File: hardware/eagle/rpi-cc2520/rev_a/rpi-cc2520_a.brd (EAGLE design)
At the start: 30.5 x 39.5 mm, 11 parts, among them J1 PINHD-2X12/SMD, J2 PINHD-2X12/SMD

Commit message: adding cc2520 and related parts
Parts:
- added C1: 1uF, rcl:C0603
- added C2, C3, C4: 100nF, rcl:C0402
- added JP2: (no value), pinhead:2X13
- added L1: (no value), SparkFun-Passives:0603
- added U1: CC2520, chips:S-PVQFN-N28
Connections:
- new net N$4: C1.1, C2.1, C3.1, C4.1, L1.1, U1.11, U1.14, U1.16, U1.20, U1.22, U1.24
- new net N$5: U1.8
- net !RESET: now also JP2.11, U1.25
- net 5V: now also JP2.2, JP2.4
- net CCA: now also JP2.15, U1.6
- net CC_GPIO0: now also U1.10
- net CC_GPIO5: now also U1.4
- net CE0: now also JP2.24, U1.3
- net CE1: now also JP2.26
- net FIFO: now also JP2.22, U1.9
- net FIFOP: now also JP2.18, U1.7
- net GND: now also C1.2, C2.2, C3.2, C4.2, JP2.14, JP2.20, JP2.25, JP2.6, JP2.9, U1.THERMALPAD
- net LED0: now also JP2.7
- net LED1: now also JP2.12
- net LED2: now also JP2.13
- net MISO: now also JP2.21, U1.1
- net MOSI: now also JP2.19, U1.2
- net SCL: now also JP2.5
- net SCLK: now also JP2.23, U1.28
- net SDA: now also JP2.3
- net SFD: now also JP2.16, U1.5
- net UART0_RXD: now also JP2.10
- net UART0_TXD: now also JP2.8
- net VCC: now also JP2.1, JP2.17, L1.2, U1.26

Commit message: working on rf path
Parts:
- added C171: 39pF, rcl:C0402
- added C172: 1.8pF, rcl:C0402
- added C191: 82pF, rcl:C0402
- renumbered C2 to C141, C3 to C151, C4 to C161
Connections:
- new net N$6: C191.2, U1.19
- new net N$7: C171.2, C172.1
- net N$4: now also C171.1, U1.17; no longer C1.1, C141.1, C151.1, C161.1, L1.1, U1.11, U1.14, U1.16, U1.20, U1.22, U1.24
- net N$5: now also C1.1, C141.1, C151.1, C161.1, L1.1, U1.11, U1.14, U1.16, U1.20, U1.22, U1.24
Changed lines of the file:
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@@
 <attribute name="DIGIKEY" value="490-1550-1-ND" x="-15.24" y="-7.62" size="1.778" layer="27" display="off"/>
 </element>
-<element name="C2" library="rcl" package="C0402" value="100nF" x="-15.24" y="-12.7">
+<element name="C141" library="rcl" package="C0402" value="100nF" x="-15.24" y="-12.7">
 <attribute name="DIGIKEY" value="490-1318-1-ND" x="-15.24" y="-12.7" size="1.778" layer="27" display="off"/>
 </element>
-<element name="C3" library="rcl" package="C0402" value="100nF" x="-15.24" y="-17.78">
+<element name="C151" library="rcl" package="C0402" value="100nF" x="-15.24" y="-17.78">
 <attribute name="DIGIKEY" value="490-1318-1-ND" x="-15.24" y="-17.78" size="1.778" layer="27" display="off"/>
 </element>
-<element name="C4" library="rcl" package="C0402" value="100nF" x="-15.24" y="-22.86">
+<element name="C161" library="rcl" package="C0402" value="100nF" x="-15.24" y="-22.86">
 <attribute name="DIGIKEY" value="490-1318-1-ND" x="-15.24" y="-22.86" size="1.778" layer="27" display="off"/>
 </element>
 <element name="L1" library="SparkFun-Passives" package="0603" value="" x="-15.24" y="-27.94">
 <attribute name="DIGIKEY" value="490-1015-1-ND" x="-15.24" y="-27.94" size="1.778" layer="27" display="off"/>
+</element>
+<element name="C171" library="rcl" package="C0402" value="39pF" x="-15.24" y="-33.02">
+<attribute name="DIGIKEY" value="490-1286-1-ND" x="-15.24" y="-33.02" size="1.778" layer="27" display="off"/>
+</element>
+<element name="C191" library="rcl" package="C0402" value="82pF" x="-15.24" y="-38.1">
+<attribute name="DIGIKEY" value="490-1290-1-ND" x="-15.24" y="-38.1" size="1.778" layer="27" display="off"/>
+</element>
+<element name="C172" library="rcl" package="C0402" value="1.8pF" x="-15.24" y="-43.18">
+<attribute name="DIGIKEY" value="399-1003-1-ND" x="-15.24" y="-43.18" size="1.778" layer="27" display="off"/>
 </element>
 </elements>
@@
 <contactref element="JP2" pad="20"/>
 <contactref element="U1" pad="THERMALPAD"/>
-<contactref element="C2" pad="2"/>
-<contactref element="C3" pad="2"/>
-<contactref element="C4" pad="2"/>
+<contactref element="C141" pad="2"/>
+<contactref element="C151" pad="2"/>
+<contactref element="C161" pad="2"/>
 <contactref element="C1" pad="2"/>
 <wire x1="16.383" y1="35.687" x2="27.813" y2="35.687" width="0" layer="19" extent="1-1"/>
@@
 <signal name="N$5">
 <contactref element="U1" pad="8"/>
-</signal>
-<signal name="N$4">
 <contactref element="U1" pad="11"/>
-<contactref element="C2" pad="1"/>
+<contactref element="C141" pad="1"/>
 <contactref element="L1" pad="1"/>
 <contactref element="U1" pad="20"/>
 <contactref element="U1" pad="24"/>
 <contactref element="U1" pad="22"/>
-<contactref element="C4" pad="1"/>
+<contactref element="C161" pad="1"/>
 <contactref element="U1" pad="14"/>
 <contactref element="U1" pad="16"/>
-<contactref element="C3" pad="1"/>
+<contactref element="C151" pad="1"/>
 <contactref element="C1" pad="1"/>
 <wire x1="-15.89" y1="-22.86" x2="-16.09" y2="-27.94" width="0" layer="19" extent="1-1"/>
@@
 <wire x1="-15.89" y1="-12.7" x2="-15.89" y2="-17.78" width="0" layer="19" extent="1-1"/>
 <wire x1="-16.09" y1="-7.62" x2="-15.89" y2="-12.7" width="0" layer="19" extent="1-1"/>
-<wire x1="-15.24" y1="0.14" x2="-16.09" y2="-7.62" width="0" layer="19" extent="1-1"/>
+<wire x1="-16.74" y1="0.14" x2="-16.09" y2="-7.62" width="0" layer="19" extent="1-1"/>
+<wire x1="-15.24" y1="0.14" x2="-16.74" y2="0.14" width="0" layer="19" extent="1-1"/>
 <wire x1="-13.74" y1="0.14" x2="-15.24" y2="0.14" width="0" layer="19" extent="1-1"/>
 <wire x1="-12.84" y1="1.54" x2="-13.74" y2="0.14" width="0" layer="19" extent="1-1"/>
@@
 <wire x1="-14.74" y1="4.94" x2="-13.74" y2="4.94" width="0" layer="19" extent="1-1"/>
 </signal>
+<signal name="N$4">
+<contactref element="U1" pad="17"/>
+<contactref element="C171" pad="1"/>
+<wire x1="-12.84" y1="2.04" x2="-15.89" y2="-33.02" width="0" layer="19" extent="1-1"/>
+</signal>
+<signal name="N$6">
+<contactref element="C191" pad="2"/>
+<contactref element="U1" pad="19"/>
+<wire x1="-12.84" y1="3.04" x2="-14.59" y2="-38.1" width="0" layer="19" extent="1-1"/>
+</signal>
+<signal name="N$7">
+<contactref element="C171" pad="2"/>
+<contactref element="C172" pad="1"/>
+<wire x1="-14.59" y1="-33.02" x2="-15.89" y2="-43.18" width="0" layer="19" extent="1-1"/>
+</signal>
 </signals>

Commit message: laying out board
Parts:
- removed EVM1: CC2520EM, brouter:TI_CC_EVM
- removed J1, J2: PINHD-2X12/SMD, headers:2X13/SMD
- added C121, C131: 27pF, rcl:C0402
- added C173: 1.8pF, rcl:C0402
- added C174: 1pF, rcl:C0402
- added C192: 1.5pF, rcl:C0402
- added C271: 100nF, rcl:C0402
- added P1: MOLEX_73251-135X, connector:SMA-J/PCB
- added R231: 56k 1%, rcl:R0402
- added R4: 1M 1%, rcl:R0402
- added X1: NX2520SA, rpi-cc2520:NX2520SA
- moved C172 68.5 mm to (18.2, 16.6), turned to 270 degrees
- moved C191 64.6 mm to (16.1, 18.4), turned to 180 degrees
- moved C171 59.4 mm to (16.1, 17.4)
- moved C161 54.5 mm to (15.6, 22.1)
- moved C151 45.1 mm to (15.6, 15.1)
- moved L1 44.0 mm to (11.7, 6.86), turned to 270 degrees
- moved U$1 35.7 mm to (39.4, 38.6)
- moved C141 35.4 mm to (8.38, 13.7), turned to 270 degrees
- moved U1 30.5 mm to (11.0, 17.9)
- moved C1 28.5 mm to (9.27, 6.86), turned to 270 degrees
- moved JP1 19.3 mm to (45.2, 19.8)
- moved JP2 8.81 mm to (3.68, 16.9)
- moved D1 6.86 mm to (10.2, 1.02)
- moved D3 6.86 mm to (20.3, 1.02)
- moved R1 6.86 mm to (10.2, 1.14)
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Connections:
- new net N$10: C174.2, P1.1
- new net N$11: C131.1, U1.13, X1.1
- new net N$12: C271.1, U1.27
- new net N$13: C121.1, U1.12, X1.3
- new net N$14: R231.2, U1.23
- new net N$8: C191.1, C192.2
- new net N$9: C173.2, C192.1
- net !RESET: no longer EVM1.P2_15, J1.12, J2.11
- net 5V: no longer J1.1, J1.3, J2.2, J2.4
- net CCA: no longer EVM1.P1_12, J1.16, J2.15
- net CC_GPIO0: no longer EVM1.P1_3
- net CC_GPIO5: no longer EVM1.P2_19
- net CE0: no longer EVM1.P1_14, J1.23, J2.24
- net CE1: no longer J1.25, J2.26
- net FIFO: no longer EVM1.P1_7, J1.21, J2.22
- net FIFOP: no longer EVM1.P1_9, J1.17, J2.18
- net GND: now also C121.2, C131.2, C172.2, C173.1, C174.1, C271.2, P1.2, P1.3, P1.4, P1.5, R231.1, R4.1; no longer EVM1.P1_1, EVM1.P1_19, J1.10, J1.13, J1.19, J1.26, J1.5, J2.14, J2.20, J2.25, J2.6, J2.9
- net LED0: no longer J1.8, J2.7
- net LED1: no longer J1.11, J2.12
- net LED2: no longer J1.14, J2.13
- net MISO: now also R4.2; no longer EVM1.P1_20, J1.22, J2.21
- net MOSI: no longer EVM1.P1_18, J1.20, J2.19
- net SCL: no longer J1.6, J2.5
- net SCLK: no longer EVM1.P1_16, J1.24, J2.23
- net SDA: no longer J1.4, J2.3
- net SFD: no longer EVM1.P2_18, J1.15, J2.16
- net UART0_RXD: no longer J1.9, J2.10
- net UART0_TXD: no longer J1.7, J2.8
- net VCC: no longer EVM1.P1_10, EVM1.P2_7, EVM1.P2_9, J1.18, J1.2, J2.1, J2.17
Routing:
- net VCC: track 98.9 -> 0.00 mm, vias 2 -> 0
- net N$5: track 0.00 -> 43.9 mm
- net LED2: track 33.4 -> 0.00 mm, vias 3 -> 0
- net FIFO: track 31.6 -> 0.00 mm, vias 1 -> 0
- net LED1: track 30.9 -> 0.00 mm, vias 3 -> 0
- net CC_GPIO0: track 28.3 -> 0.00 mm
- net SFD: track 31.3 -> 7.08 mm, vias 2 -> 0
- net CCA: track 28.3 -> 4.74 mm, vias 2 -> 1
- net FIFOP: track 35.5 -> 12.0 mm, vias 1 -> 0
- net GND: track 22.9 -> 0.00 mm, vias 5 -> 9
- net !RESET: track 20.5 -> 0.00 mm, vias 1 -> 0
- net MOSI: track 20.5 -> 0.00 mm, vias 1 -> 0
- net LED0: track 17.3 -> 0.00 mm, vias 2 -> 0
- net MISO: track 16.8 -> 0.00 mm, vias 1 -> 0
- net CC_GPIO5: track 15.6 -> 0.00 mm, vias 2 -> 0
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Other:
- board size 30.5 x 39.5 mm -> 27.3 x 33.8 mm

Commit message: updated bom with digikey part numbers
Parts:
- R1, R2, R3: value (none) -> 470
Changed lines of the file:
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@@
 <attribute name="NAME" x="10.16" y="1.651" size="1.016" layer="25" font="vector" ratio="12" align="bottom-center"/>
 <attribute name="VALUE" x="9.144" y="-0.0635" size="0.4064" layer="27"/>
+<attribute name="DIGIKEY" value="160-1834-1-ND" x="10.16" y="1.016" size="1.778" layer="27" rot="R270" display="off"/>
 </element>
 <element name="D2" library="SparkFun-LED" package="LED-0603" value="" x="15.24" y="1.016" smashed="yes" rot="R270">
 <attribute name="NAME" x="15.24" y="1.651" size="1.016" layer="25" font="vector" ratio="12" align="bottom-center"/>
 <attribute name="VALUE" x="14.224" y="-0.0635" size="0.4064" layer="27"/>
+<attribute name="DIGIKEY" value="160-1835-1-ND" x="15.24" y="1.016" size="1.778" layer="27" rot="R270" display="off"/>
 </element>
 <element name="D3" library="SparkFun-LED" package="LED-0603" value="" x="20.32" y="1.016" smashed="yes" rot="R270">
 <attribute name="NAME" x="20.32" y="1.651" size="1.016" layer="25" font="vector" ratio="12" align="bottom-center"/>
 <attribute name="VALUE" x="19.304" y="-0.0635" size="0.4064" layer="27"/>
+<attribute name="DIGIKEY" value="160-1837-1-ND" x="20.32" y="1.016" size="1.778" layer="27" rot="R270" display="off"/>
 </element>
-<element name="R1" library="rcl" package="R0603" value="" x="10.16" y="1.143" smashed="yes" rot="MR180">
+<element name="R1" library="rcl" package="R0603" value="470" x="10.16" y="1.143" smashed="yes" rot="MR180">
 <attribute name="NAME" x="10.16" y="1.905" size="1.016" layer="26" font="vector" ratio="12" rot="MR180" align="top-center"/>
 <attribute name="VALUE" x="9.525" y="3.048" size="1.27" layer="28" rot="MR180"/>
 </element>
-<element name="R2" library="rcl" package="R0603" value="" x="15.24" y="1.143" smashed="yes" rot="MR180">
+<element name="R2" library="rcl" package="R0603" value="470" x="15.24" y="1.143" smashed="yes" rot="MR180">
 <attribute name="NAME" x="15.24" y="1.905" size="1.016" layer="26" font="vector" ratio="12" rot="MR180" align="top-center"/>
 <attribute name="VALUE" x="14.605" y="3.048" size="1.27" layer="28" rot="MR180"/>
 </element>
-<element name="R3" library="rcl" package="R0603" value="" x="20.32" y="1.143" smashed="yes" rot="MR180">
+<element name="R3" library="rcl" package="R0603" value="470" x="20.32" y="1.143" smashed="yes" rot="MR180">
 <attribute name="NAME" x="20.32" y="1.905" size="1.016" layer="26" font="vector" ratio="12" rot="MR180" align="top-center"/>
 <attribute name="VALUE" x="19.685" y="3.048" size="1.27" layer="28" rot="MR180"/>

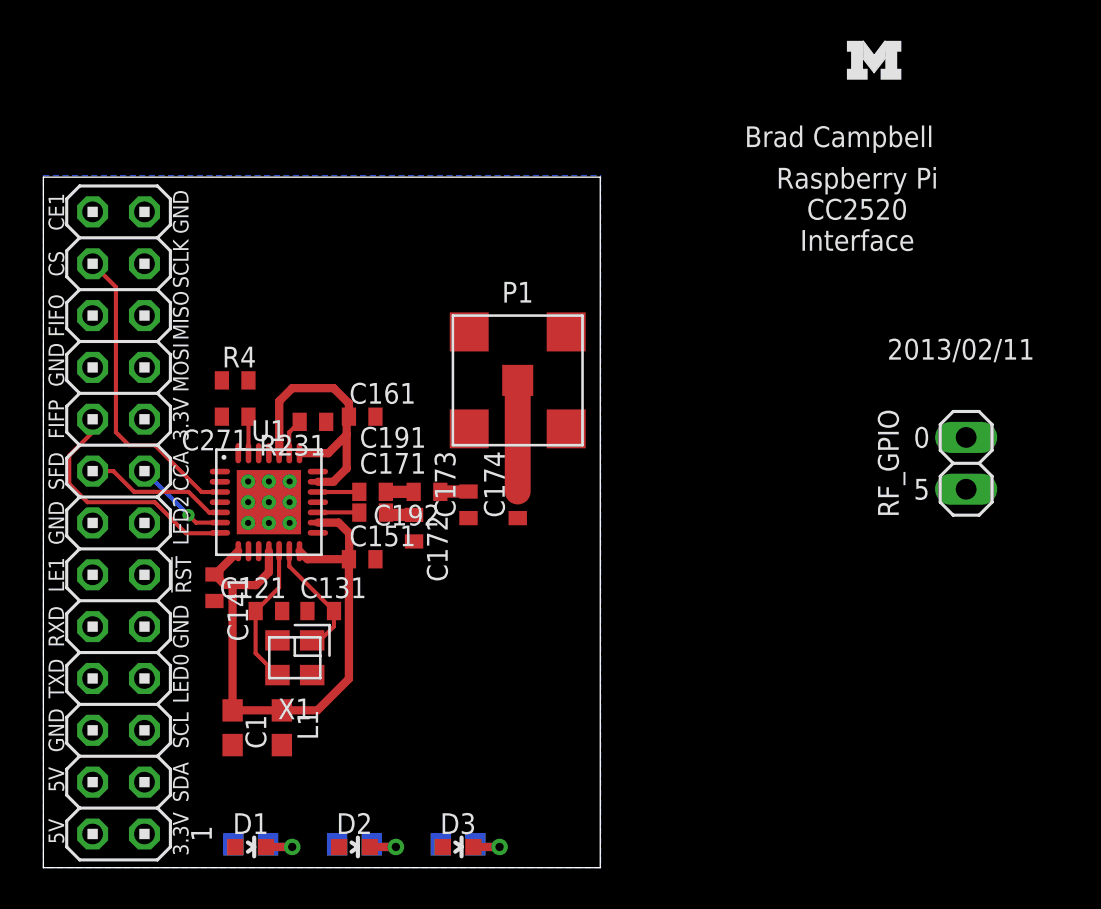
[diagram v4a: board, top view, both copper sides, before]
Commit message: carefully laying out the sma antenna
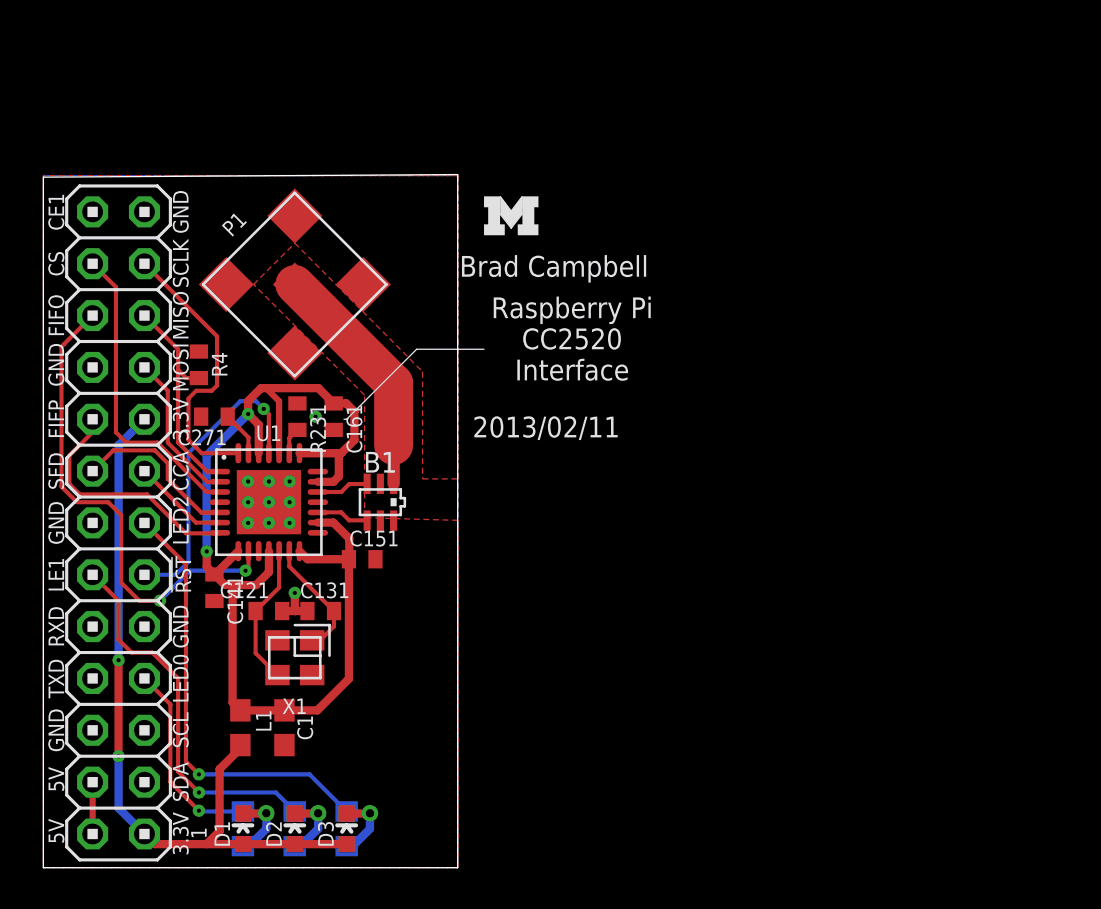
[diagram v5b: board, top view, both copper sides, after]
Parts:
- removed C171: 39pF, rcl:C0402
- removed C172, C173: 1.8pF, rcl:C0402
- removed C174: 1pF, rcl:C0402
- removed C191: 82pF, rcl:C0402
- removed C192: 1.5pF, rcl:C0402
- removed JP1: (no value), pinhead:1X02
- added B1: 2450BM15A0002, rpi-cc2520:2450BM
- moved U$1 19.3 mm to (21.6, 31.0)
- moved P1 11.9 mm to (12.3, 28.6), turned to 45 degrees
- moved D3 5.53 mm to (14.9, 1.91), turned to 0 degrees
- moved R3 5.51 mm to (14.9, 1.91), turned to 270 degrees
- moved D2 3.05 mm to (12.3, 1.91), turned to 0 degrees
- moved R2 3.02 mm to (12.3, 1.91), turned to 270 degrees
- moved C1 2.54 mm to (11.8, 6.86)
- moved L1 2.03 mm to (9.65, 6.86)
- moved R4 1.93 mm to (7.62, 24.6), turned to 270 degrees
- moved C161 1.40 mm to (14.2, 22.1), turned to 270 degrees
- moved C271 1.02 mm to (8.38, 22.1)
- moved D1 0.97 mm to (9.78, 1.91), turned to 0 degrees
- moved R1 0.85 mm to (9.78, 1.91), turned to 270 degrees
- moved R231 0.80 mm to (12.4, 22.1), turned to 270 degrees
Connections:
- removed net N$10: C174.2, P1.1
- removed net N$4: C171.1, U1.17
- removed net N$6: C191.2, U1.19
- removed net N$8: C191.1, C192.2
- removed net N$9: C173.2, C192.1
- new net RF_N: B1.3, U1.19
- new net RF_P: B1.4, U1.17
- net CC_GPIO0: no longer JP1.2
- net CC_GPIO5: no longer JP1.1
- net GND: now also B1.2, B1.5, B1.6; no longer C172.2, C173.1, C174.1
- net N$5: now also U1.26
- net N$7: now also B1.1, P1.1; no longer C171.2, C172.1
- net VCC: no longer U1.26
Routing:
- net VCC: track 0.00 -> 37.0 mm, vias 0 -> 2
- net FIFO: track 0.00 -> 23.9 mm, vias 0 -> 2
- net LED2: track 0.00 -> 21.4 mm, vias 0 -> 1
- net LED1: track 0.00 -> 18.5 mm, vias 0 -> 1
- net !RESET: track 0.00 -> 14.9 mm, vias 0 -> 1
- net SCLK: track 0.00 -> 13.8 mm
- net N$5: track 43.9 -> 57.0 mm, vias 0 -> 2
- net MISO: track 0.00 -> 10.7 mm
- net N$7: track 1.43 -> 11.8 mm
- net LED0: track 0.00 -> 9.76 mm, vias 0 -> 1
- net MOSI: track 0.00 -> 7.51 mm
- net N$10: track 5.45 -> 0.00 mm
- net RF_P: track 0.00 -> 2.58 mm
- net RF_N: track 0.00 -> 2.58 mm
- net 5V: track 0.00 -> 2.54 mm
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- added copper zone on layer 1, net GND
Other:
- board size 27.3 x 33.8 mm -> 20.3 x 34 mm
- board text removed: "0"
- board text removed: "5"
- board text removed: "RF_GPIO"
